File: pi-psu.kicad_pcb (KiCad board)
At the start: 2 copper layers, 80 x 40 mm, 23 parts, among them Q1 j113, Q2 PNP, Q3 NPN

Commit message: moved active
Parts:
- moved C4 14.6 mm to (183.0, 70.0)
- moved D6 10.5 mm to (170.0, 74.0)
- moved Q3 9.93 mm to (170.0, 84.9)
- moved Q1 9.92 mm to (164.5, 89.9)
- moved Q2 9.92 mm to (170.0, 60.0)
- moved R1 9.92 mm to (168.0, 89.9)
- moved R3 9.92 mm to (165.0, 84.4)
- moved C3 9.47 mm to (177.3, 89.5)
- moved R2 8.39 mm to (172.5, 88.2), turned to 0 degrees
- moved D5 7.43 mm to (172.5, 91.0)
- moved I1 5.00 mm to (186.8, 76.5)
- moved R4 2.93 mm to (188.0, 68.2), turned to 90 degrees
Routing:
- net out: track 48.7 -> 38.6 mm
- net pre-reg: track 83.4 -> 92.3 mm
- net GND: track 15.1 -> 6.43 mm
- net vref: track 10.1 -> 11.1 mm
- net zener-in: track 11.5 -> 10.8 mm
- added copper zone on B.Cu, net ac
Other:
- outline, holes or cut-outs redrawn

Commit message: cleaned up front silk screen
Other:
- board text added: "+"
- board text added: "-"
- board text added: "ac"
- board text added: "pi-psu | cibo l-adapter + aya"
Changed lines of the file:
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@@
 		(tags "Diode SMC (DO-214AB)")
 		(property "Reference" "D3"
-			(at 0 -4.1 0)
+			(at -0.15 -4.05 0)
 			(layer "F.SilkS")
 			(effects
@@
 		(tags "CP Radial series Radial pin pitch 7.50mm  diameter 18mm Electrolytic Capacitor")
 		(property "Reference" "C2"
-			(at 3.75 -15.45 90)
+			(at -2.52222 -8.1 0)
 			(layer "F.SilkS")
 			(effects
@@
 			(at 2.54 -0.2 90)
 			(layer "F.SilkS")
+			(hide yes)
 			(effects
 				(font
@@
 		(tags "resistor")
 		(property "Reference" "R2"
-			(at 0 -1.82 0)
+			(at -3.4 -1.15 0)
 			(layer "F.SilkS")
 			(effects
@@
 		(tags "CP Radial series Radial pin pitch 2.00mm  diameter 5mm Electrolytic Capacitor")
 		(property "Reference" "C3"
-			(at 1 -3.75 0)
+			(at 0.805112 3.7 0)
 			(layer "F.SilkS")
 			(effects
@@
 			(at 0 -3.85 0)
 			(layer "F.SilkS")
+			(hide yes)
 			(effects
 				(font
@@
 		(tags "CP Radial series Radial pin pitch 2.00mm  diameter 5mm Electrolytic Capacitor")
 		(property "Reference" "C4"
-			(at 1 -3.75 0)
+			(at 1 3.6 0)
 			(layer "F.SilkS")
 			(effects
@@
 		(tags "resistor")
 		(property "Reference" "R4"
-			(at 0 -2.62 90)
+			(at 0 3.1 0)
 			(layer "F.SilkS")
 			(effects
@@
 			(at 0 -3.85 0)
 			(layer "F.SilkS")
+			(hide yes)
 			(effects
 				(font
@@
 		(tags "Diode SMC (DO-214AB)")
 		(property "Reference" "D4"
-			(at 0 -4.1 0)
+			(at 0 4.35 0)
 			(layer "F.SilkS")
 			(effects
@@
 		(tags "resistor")
 		(property "Reference" "R3"
-			(at 0 -1.82 90)
+			(at 3.275 0 0)
 			(layer "F.SilkS")
 			(effects
@@
 		(tags "Diode SMC (DO-214AB)")
 		(property "Reference" "D2"
-			(at 0 -4.1 0)
+			(at -0.05 4.25 0)
 			(layer "F.SilkS")
 			(effects
@@
 		(tags "TO-3P-3 Horizontal RM 5.45mm ")
 		(property "Reference" "Q2"
-			(at 0 -5.32 0)
+			(at -2.5 19.2 0)
 			(layer "F.SilkS")
 			(effects
@@
 		(tags "CP Radial series Radial pin pitch 7.50mm  diameter 18mm Electrolytic Capacitor")
 		(property "Reference" "C1"
-			(at 3.75 -10.25 90)
+			(at -2.62222 -8.3 0)
 			(layer "F.SilkS")
 			(effects
@@
 		(tags "SOT TO_SOT_SMD")
 		(property "Reference" "Q1"
-			(at 0 -2.4 0)
+			(at 0 3.075 0)
 			(layer "F.SilkS")
 			(effects
@@
 			(at 0 -3.85 0)
 			(layer "F.SilkS")
+			(hide yes)
 			(effects
 				(font
@@
 		(tags "Diode Mini-MELF (SOD-80)")
 		(property "Reference" "D5"
-			(at 0 -2 0)
+			(at -0.1 2 0)
 			(layer "F.SilkS")
 			(effects
@@
 			(at 0 -3.85 0)
 			(layer "F.SilkS")
+			(hide yes)
 			(effects
 				(font
@@
 		(tags "resistor")
 		(property "Reference" "R1"
-			(at 0 -1.82 90)
+			(at 3.075 0 0)
 			(layer "F.SilkS")
 			(effects
@@
 		(tags "Diode SMC (DO-214AB)")
 		(property "Reference" "D1"
-			(at 0 -4.1 0)
+			(at -0.05 -4.05 0)
 			(layer "F.SilkS")
 			(effects
@@
 		(layer "Edge.Cuts")
 	)
+	(gr_text "-\n"
+		(at 193 82.3 0)
+		(layer "F.SilkS")
+		(effects
+			(font
+				(size 1 1)
+				(thickness 0.1)
+			)
+			(justify left bottom)
+		)
+	)
+	(gr_text "ac"
+		(at 116 87 0)
+		(layer "F.SilkS")
+		(effects
+			(font
+				(size 1 1)
+				(thickness 0.1)
+			)
+			(justify left bottom)
+		)
+	)
+	(gr_text "+"
+		(at 192.9 76.8 0)
+		(layer "F.SilkS")
+		(effects
+			(font
+				(size 1 1)
+				(thickness 0.1)
+			)
+			(justify left bottom)
+		)
+	)
+	(gr_text "pi-psu | cibo \nl-adapter + aya"
+		(at 169.9 69.9 0)
+		(layer "F.SilkS")
+		(effects
+			(font
+				(size 1 1)
+				(thickness 0.1)
+			)
+			(justify bottom)
+		)
+	)
 	(segment

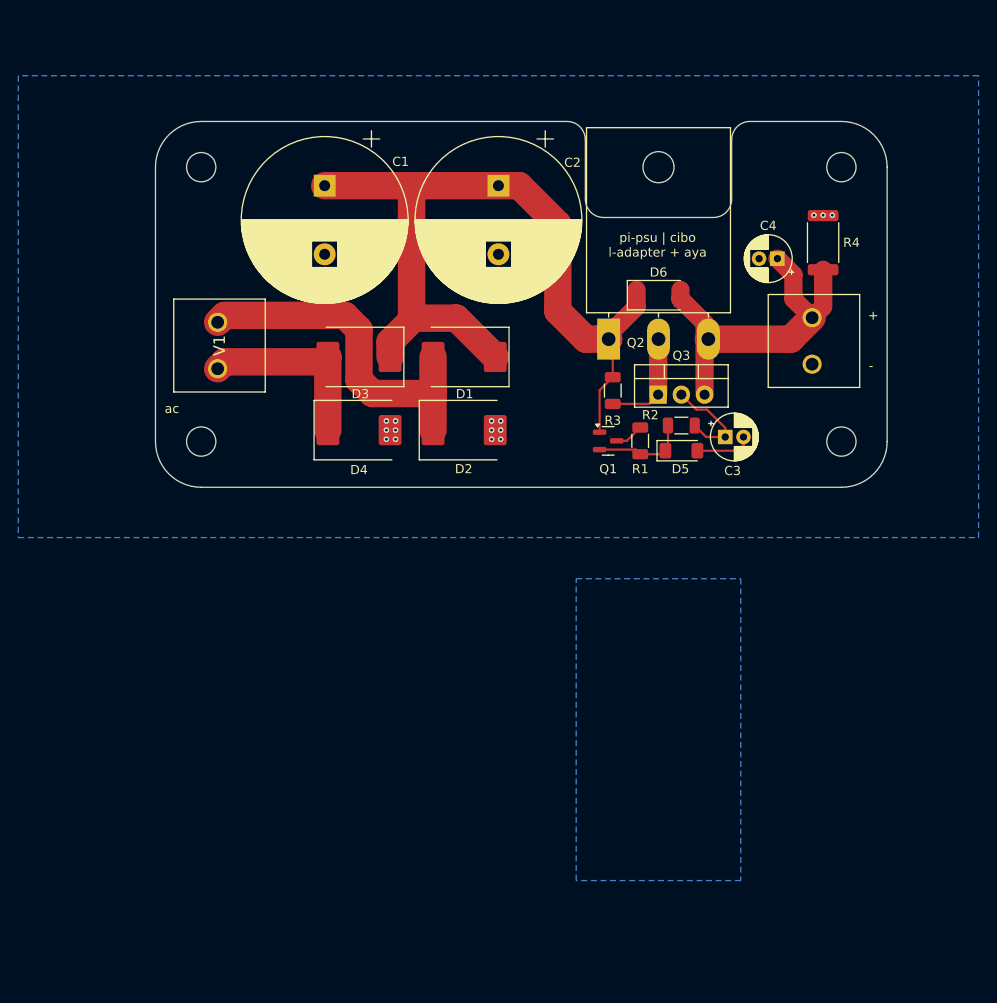
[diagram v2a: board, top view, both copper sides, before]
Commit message: made power traces 4mm
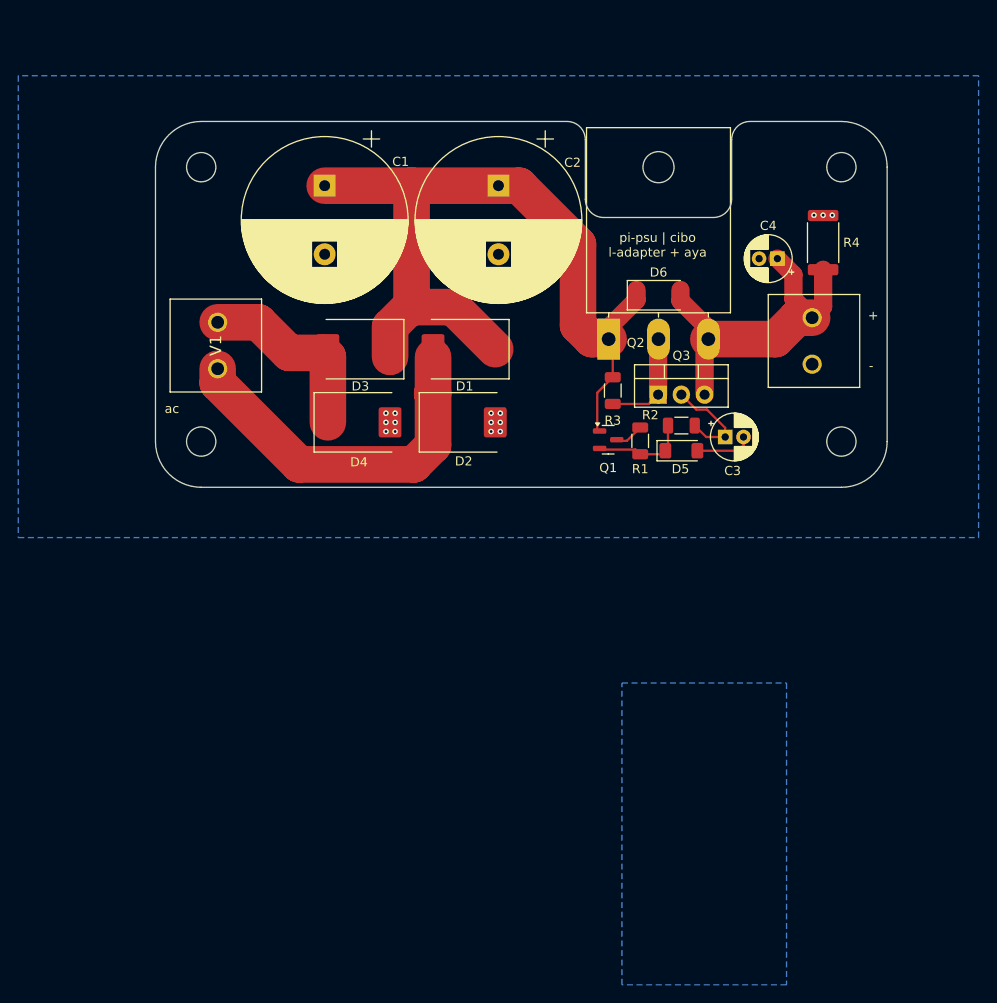
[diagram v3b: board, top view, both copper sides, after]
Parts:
- moved V1 5.08 mm to (121.8, 82.0), turned to 90 degrees
- moved D1 0.85 mm to (148.8, 79.9)
- moved D2 0.85 mm to (148.8, 87.9)
- moved D3 0.85 mm to (137.2, 79.9)
- moved D4 0.85 mm to (137.2, 87.9)
- moved Q1 0.12 mm to (164.5, 89.8)
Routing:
- net Net-(D1-A): track 38.6 -> 39.4 mm

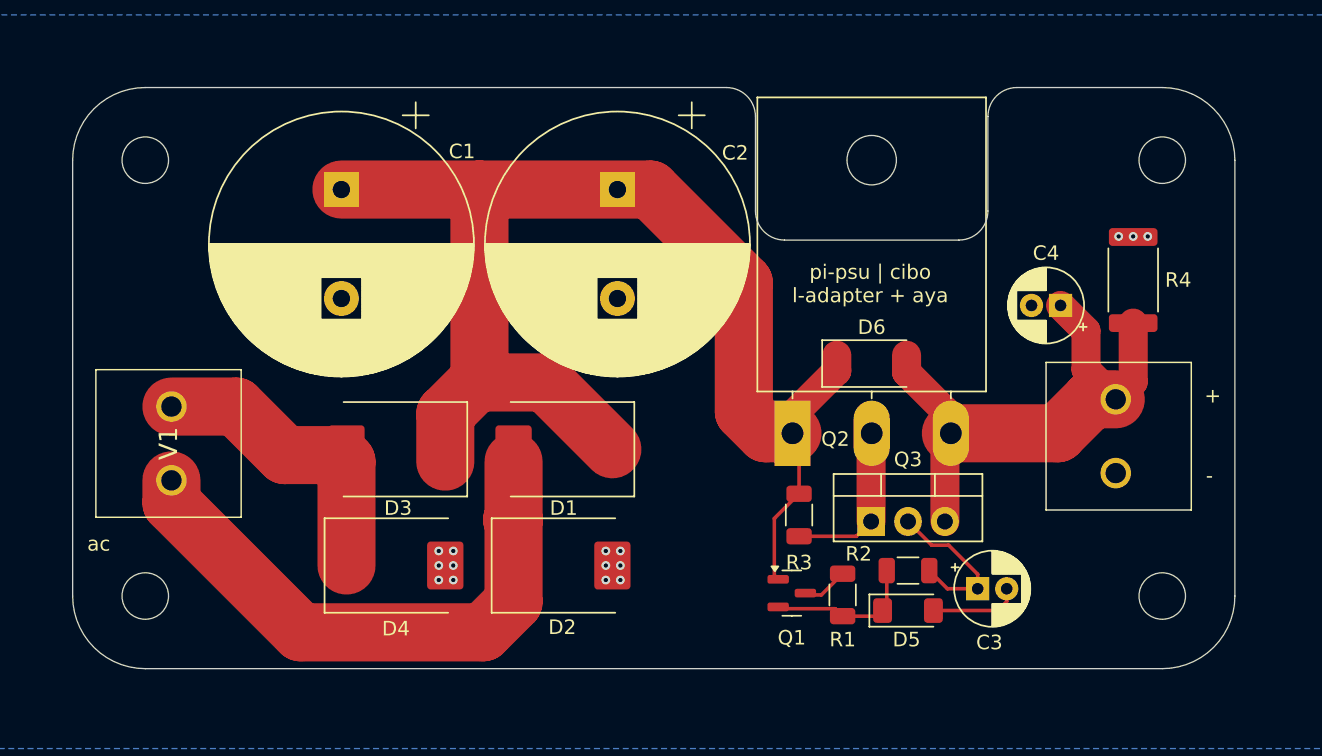
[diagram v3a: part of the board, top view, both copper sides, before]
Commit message: doenst work with tip41 and 41
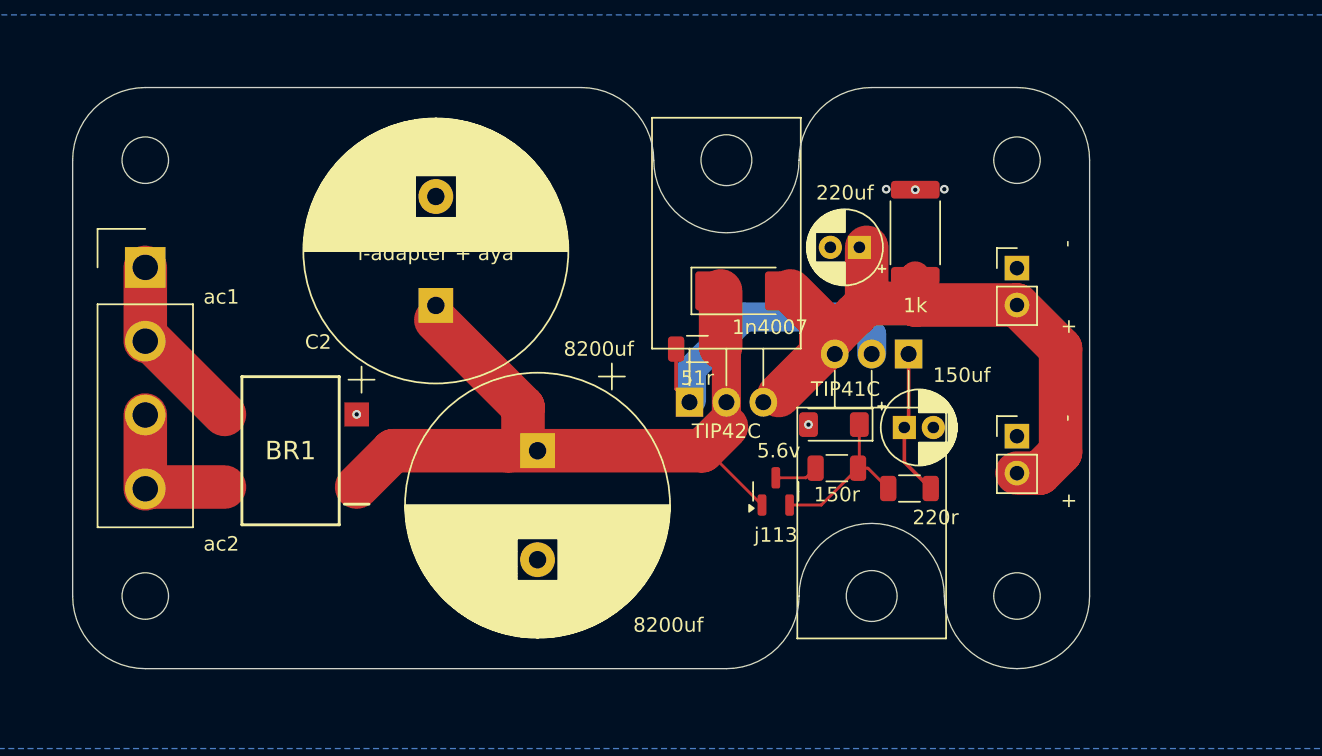
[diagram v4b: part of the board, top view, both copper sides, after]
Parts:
- removed D1, D2, D3, D4: D_Schottky, Diode_SMD:D_SMC
- removed I1: 3, Samacsys:395443002
- removed Q2: PNP, Package_TO_SOT_THT:TO-3P-3_Horizontal_TabDown
- removed V1: VSIN, Samacsys:395443002
- added BR1: RTT410, Samacsys:SOP500P990X180-4N, F.Cu at (130.0, 80.0)
- added J1: Conn_02x01, Connector_PinHeader_2.54mm:PinHeader_1x02_P2.54mm_Vertical, F.Cu at (180.0, 67.4)
- added J2: Conn_02x01, Connector_PinHeader_2.54mm:PinHeader_1x02_P2.54mm_Vertical, F.Cu at (180.0, 79.0)
- added J3: Conn_01x04_Pin, Connector_Samtec_HPM_THT:Samtec_HPM-04-01-x-S_Straight_1x04_Pitch5.08mm, F.Cu at (120.0, 67.4)
- added Q4: TIP41C, Package_TO_SOT_THT:TO-220-3_Horizontal_TabDown, F.Cu at (170.0, 90.0)
- Q3: value NPN -> TIP42C; footprint Package_TO_SOT_THT:TO-220-3_Vertical -> Package_TO_SOT_THT:TO-220-3_Horizontal_TabDown
- moved Q3 26.8 mm to (160.0, 60.0)
- moved C1 22.5 mm to (147.0, 80.0)
- moved R4 15.3 mm to (173.0, 65.0)
- moved C2 14.8 mm to (140.0, 70.0), turned to 90 degrees
- moved C4 14.4 mm to (169.2, 66.0)
- moved D5 13.8 mm to (167.4, 78.2), turned to 180 degrees
- moved R3 13.4 mm to (158.0, 73.0), turned to 180 degrees
- moved C3 12.2 mm to (172.2, 78.4)
- moved D6 10.3 mm to (161.0, 69.0)
- moved H2 10.0 mm to (180.0, 60.0)
- moved H3 10.0 mm to (180.0, 90.0)
- moved R1 8.73 mm to (167.6, 81.2), turned to 0 degrees
- moved Q1 7.09 mm to (163.4, 82.8), turned to 90 degrees
- moved R2 5.65 mm to (172.6, 82.6)
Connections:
- Q3 pad 2: vref -> pre-reg
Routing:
- net Net-(D1-A): track 39.4 -> 0.00 mm
- net pre-reg: track 92.4 -> 56.6 mm
- net Net-(BR1-~_1): track 0.00 -> 12.6 mm
- net ac: track 20.8 -> 10.6 mm
- net Net-(Q3-B): track 12.0 -> 21.9 mm
- net out: track 38.6 -> 45.1 mm
- net GND: track 6.43 -> 0.00 mm, vias 15 -> 5
- net zener-in: track 10.8 -> 11.5 mm
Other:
- board size 80 x 40 mm -> 70 x 40 mm
- board text added: "ac1"
- board text added: "ac2"
- board text removed: "ac"

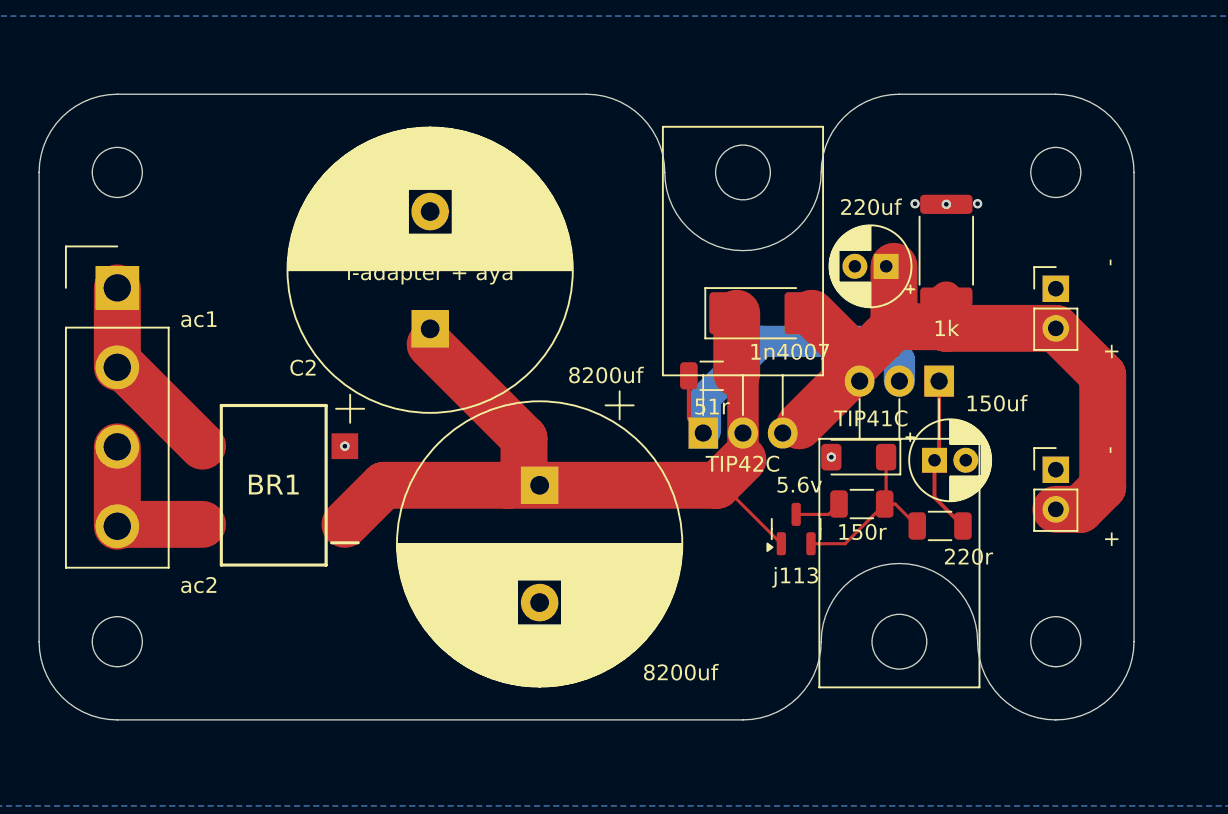
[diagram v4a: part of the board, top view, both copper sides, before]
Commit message: sims well, sending to jlc
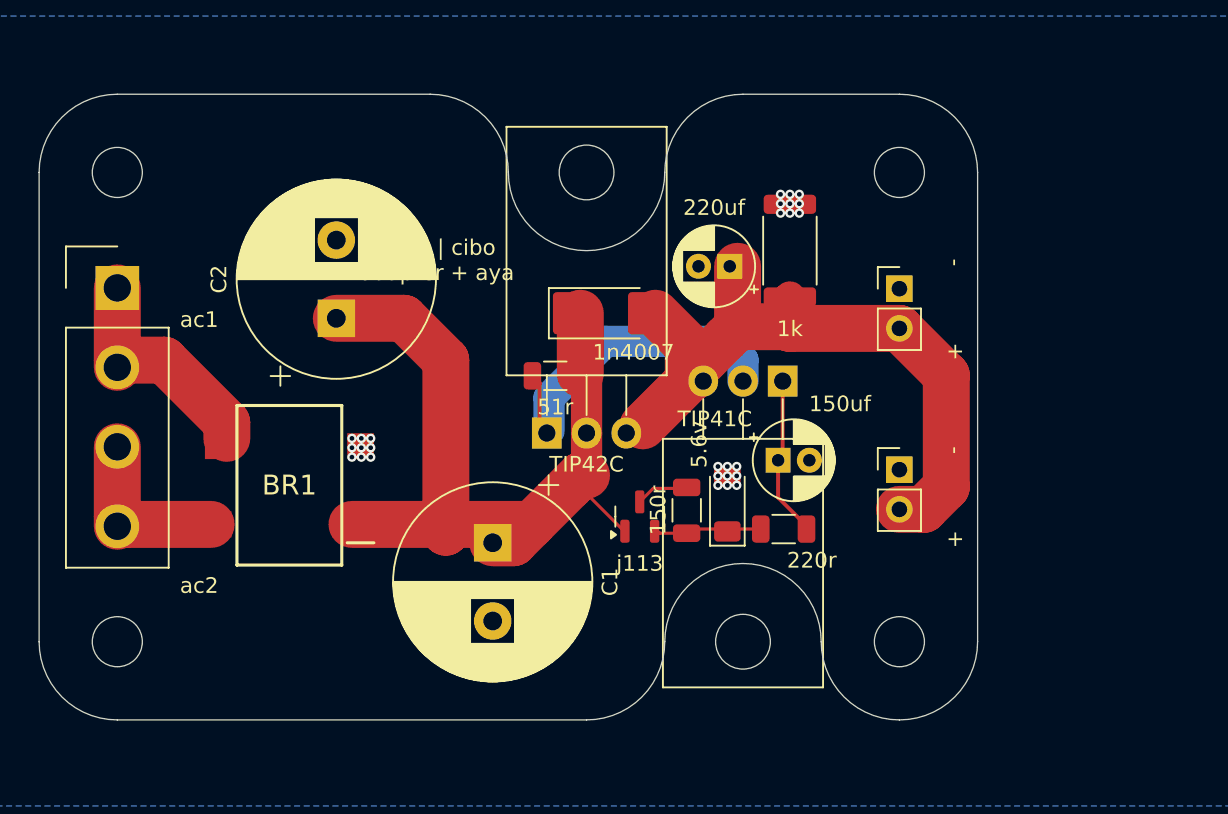
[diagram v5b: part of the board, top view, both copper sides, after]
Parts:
- C1, C2: value 8200uf -> 4700uf; footprint Capacitor_THT:CP_Radial_D18.0mm_P7.50mm -> Capacitor_THT:CP_Radial_D12.5mm_P5.00mm
- moved R1 11.2 mm to (156.4, 81.6), turned to -90 degrees
- moved Q1 10.0 mm to (153.4, 82.0)
- moved R2 10.0 mm to (162.6, 82.8)
- moved C3 10.0 mm to (162.2, 78.4)
- moved C4 10.0 mm to (159.2, 66.0)
- moved D6 10.0 mm to (151.0, 69.0)
- moved H2 10.0 mm to (170.0, 60.0)
- moved H3 10.0 mm to (170.0, 90.0)
- moved P1 10.0 mm to (170.0, 79.0)
- moved P2 10.0 mm to (170.0, 67.4)
- moved Q3 10.0 mm to (150.0, 60.0)
- moved Q4 10.0 mm to (160.0, 90.0)
- moved R3 10.0 mm to (148.0, 73.0)
- moved R4 10.0 mm to (163.0, 65.0)
- moved D5 8.92 mm to (159.0, 81.2), turned to 90 degrees
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- renumbered J2 to P1, J1 to P2, J3 to P3
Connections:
- BR1 pad 2: GND -> (no net)
- C1 pad 2: GND -> 0
- C2 pad 2: GND -> 0
- C3 pad 2: GND -> 0
- C4 pad 2: GND -> 0
- D5 pad 2: GND -> 0
- P1 pad 1: GND -> 0
- P2 pad 1: GND -> 0
- Q3 pad 2: pre-reg -> out
- Q3 pad 3: out -> pre-reg
- R4 pad 2: GND -> 0
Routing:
- net zener-in: track 11.5 -> 6.93 mm
- net Net-(BR1-~_1): track 12.6 -> 15.1 mm
- net pre-reg: track 56.6 -> 54.5 mm
- net ac: track 10.6 -> 11.5 mm
- net GND: vias 5 -> 0
- net 0: vias 0 -> 27
- added copper zone on B.Cu, net 0
- removed copper zone on B.Cu, net GND
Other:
- board size 70 x 40 mm -> 60 x 40 mm
